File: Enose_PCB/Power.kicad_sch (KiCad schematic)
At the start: 53 parts, among them IC1 ISL91127IRNZ-T7A, IC2 MP2722GRH-0000-Z, J5 USB_C_Receptacle_USB2.0_16P, J6 Battery Terminal, SW3 SW_DPST_x2, U2 USBLC6-4SC6

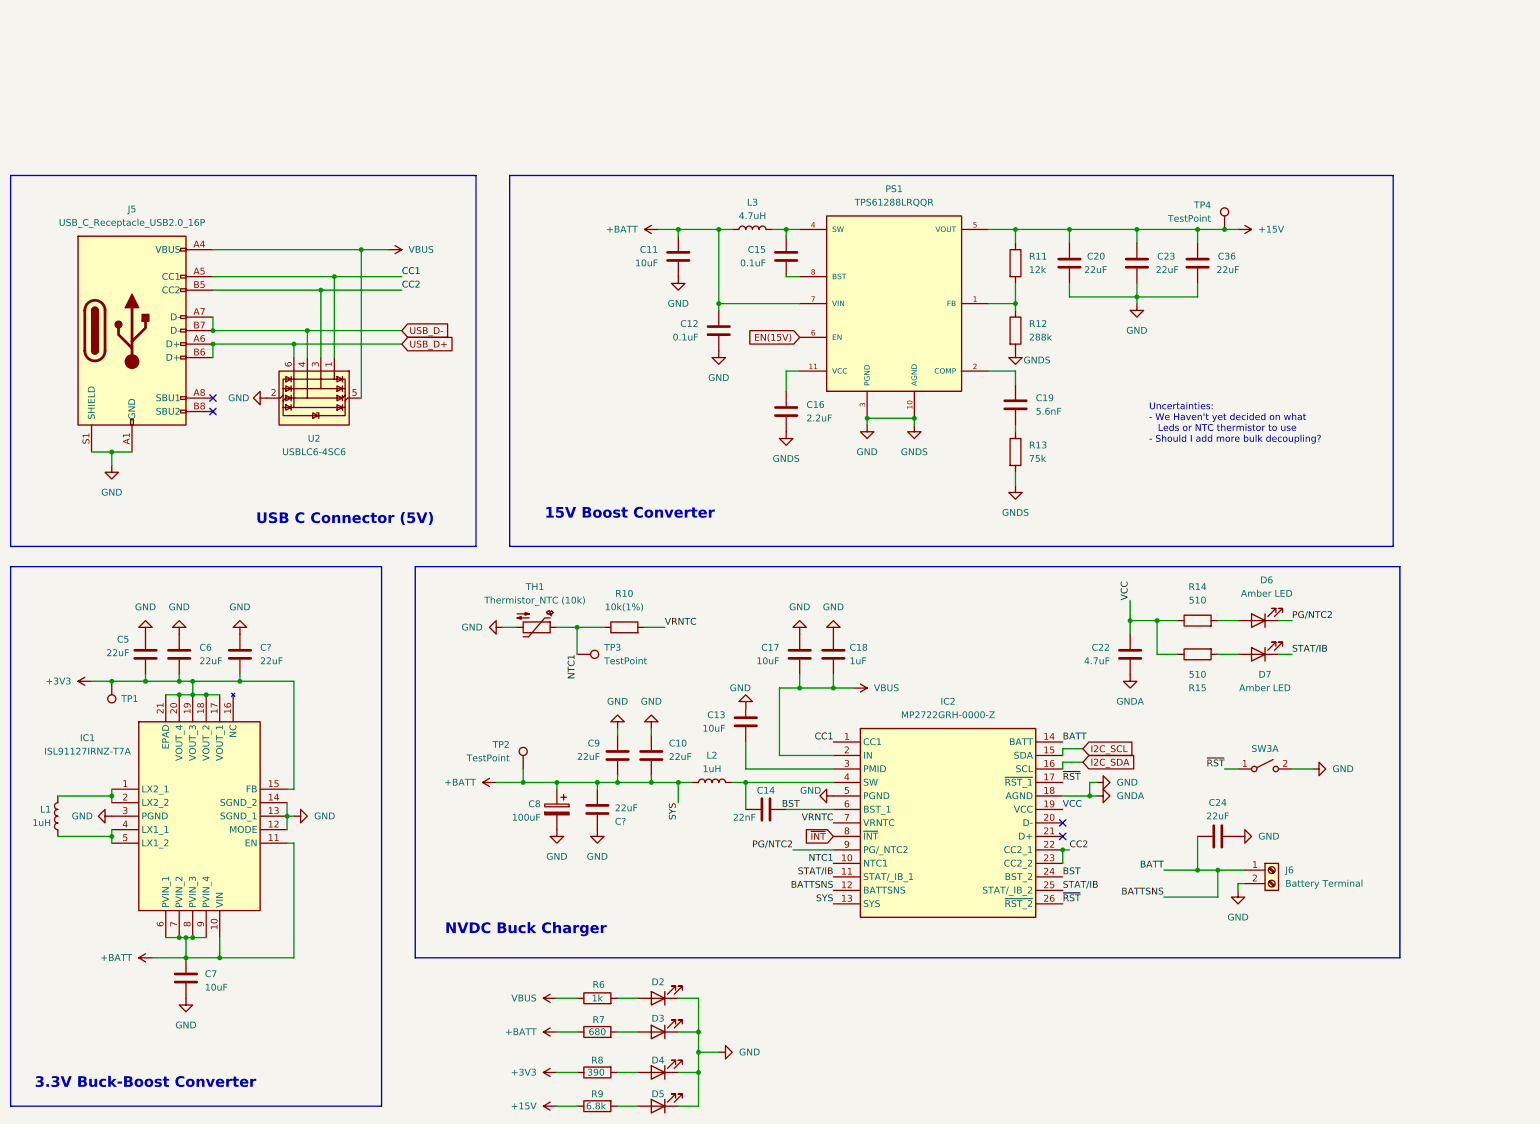
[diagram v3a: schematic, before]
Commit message: Added load switch and stuff
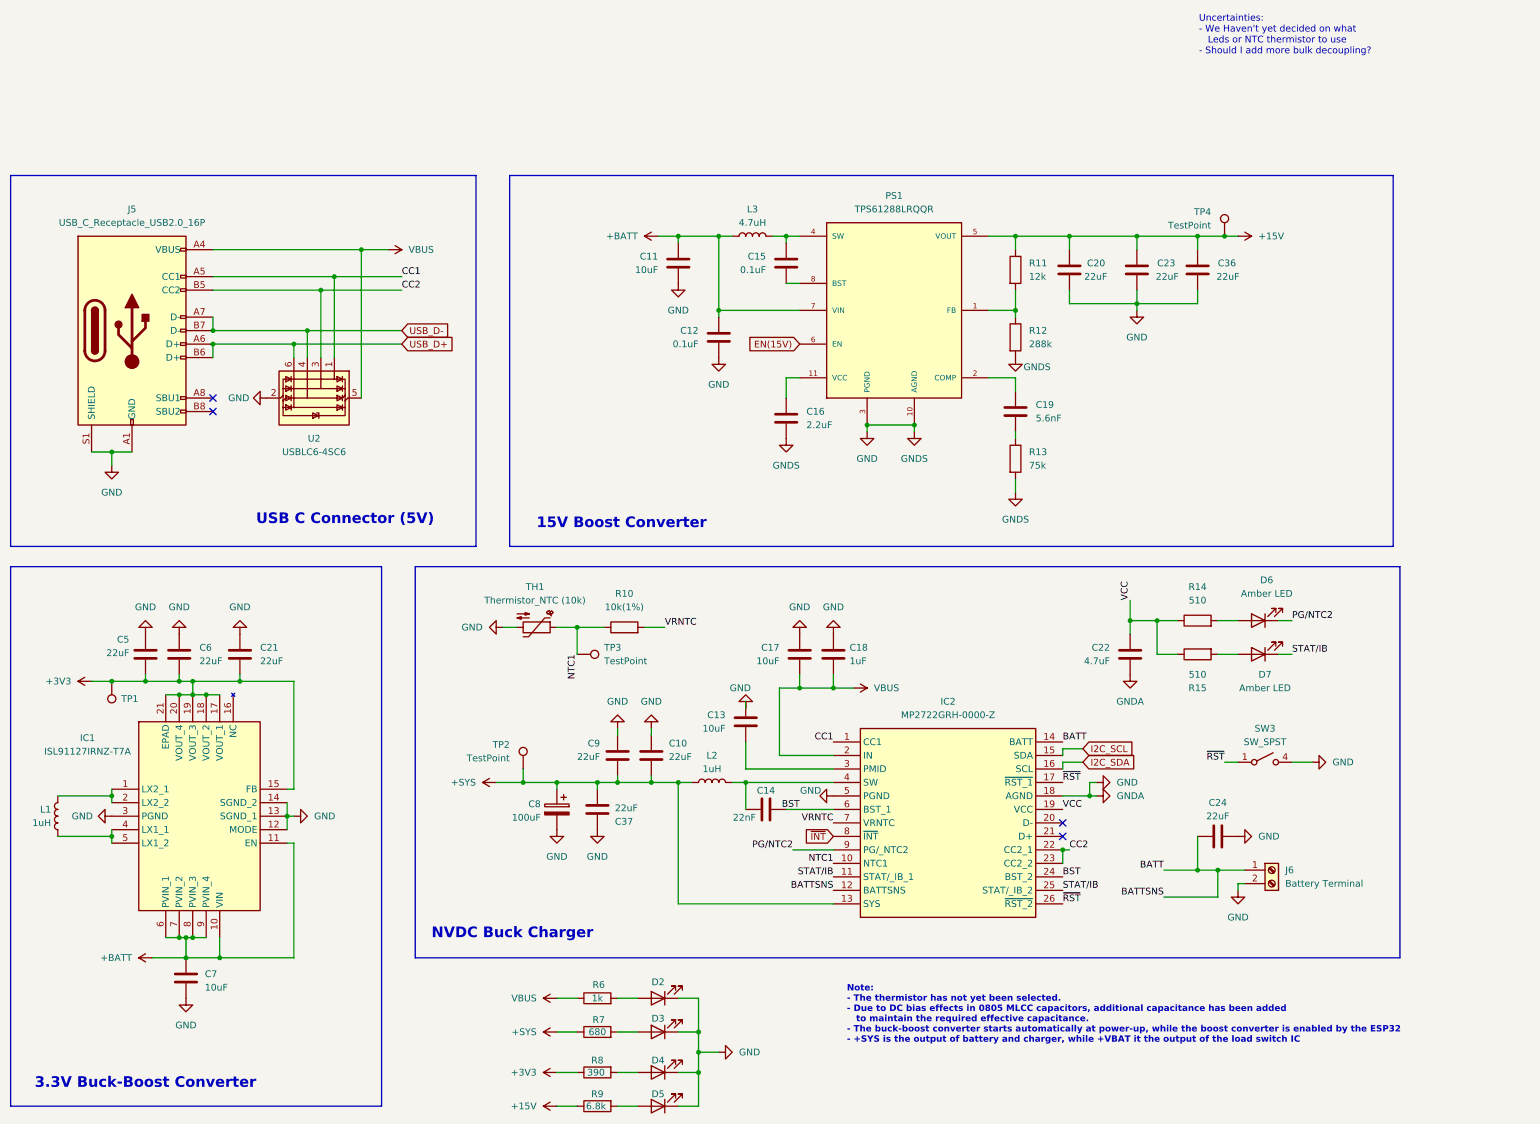
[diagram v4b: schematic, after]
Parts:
- removed SW3: SW_DPST_x2, symbol Switch:SW_DPST_x2
- added SW3: SW_SPST, SamacSys_Parts:430181038816, symbol Switch:SW_SPST
- C10: footprint Capacitor_SMD:C_0805_2012Metric -> Capacitor_SMD:C_0805_2012Metric_Pad1.18x1.45mm_HandSolder
- C11, C12, C13, C14, C15, C16, C17, C18, C19, C22, C24, C5, C6, C7, C9: footprint (none) -> Capacitor_SMD:C_0805_2012Metric_Pad1.18x1.45mm_HandSolder
- C20, C23: footprint Capacitor_SMD:C_1210_3225Metric -> Capacitor_SMD:C_1210_3225Metric_Pad1.33x2.70mm_HandSolder
- C21, C37: renamed from C?; footprint (none) -> Capacitor_SMD:C_0805_2012Metric_Pad1.18x1.45mm_HandSolder
- C36: footprint Capacitor_THT:C_Disc_D6.0mm_W4.4mm_P5.00mm -> Capacitor_SMD:C_1210_3225Metric_Pad1.33x2.70mm_HandSolder
- C8: footprint (none) -> SamacSys_Parts:CAPAE530X610N
- D2, D3, D4, D5, D6, D7: footprint (none) -> LED_SMD:LED_0805_2012Metric_Pad1.15x1.40mm_HandSolder
- IC1: footprint QFN50P400X400X100-21N -> ISL91127IRNZ-T7A:QFN50P400X400X100-21N
- IC2: footprint MP2722GRH0000Z -> SamacSys_Parts:MP2722GRH0000Z
- R10, R11, R12, R13, R14, R15, R6, R7, R8, R9: footprint (none) -> Resistor_SMD:R_0805_2012Metric_Pad1.20x1.40mm_HandSolder
- TP1, TP2, TP3, TP4: footprint (none) -> TestPoint:TestPoint_Pad_1.5x1.5mm
- U2: footprint Package_TO_SOT_SMD:SOT-23-6 -> Package_TO_SOT_SMD:SOT-23-6_Handsoldering
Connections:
- net +BATT: no longer C10.2, C37.1, C8.1, C9.1, IC2.13 (SYS), L2.1, R7.1, TP2.1
- net GND: now also SW3.4 (B)
- net ~{RST}: now also SW3.1 (A)
- new net +SYS: C10.2, C37.1, C8.1, C9.1, IC2.13 (SYS), L2.1, R7.1, TP2.1
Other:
- note added: "Note: - The thermistor has not yet been selected. - Due to DC bias effects in 0805 MLCC capacitors, additional capacitance has been added to maintain the required effective capacitance. - The buck-boost converter starts automatically at power-up, while the boost converter is enabled by the ESP32 - +SYS is the output of battery and charger, while +VBAT it the output of the load switch IC"
- moved on the sheet: C11, C12, C15, C16, C19, C20, C23, C36, L3, PS1, R11, R12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

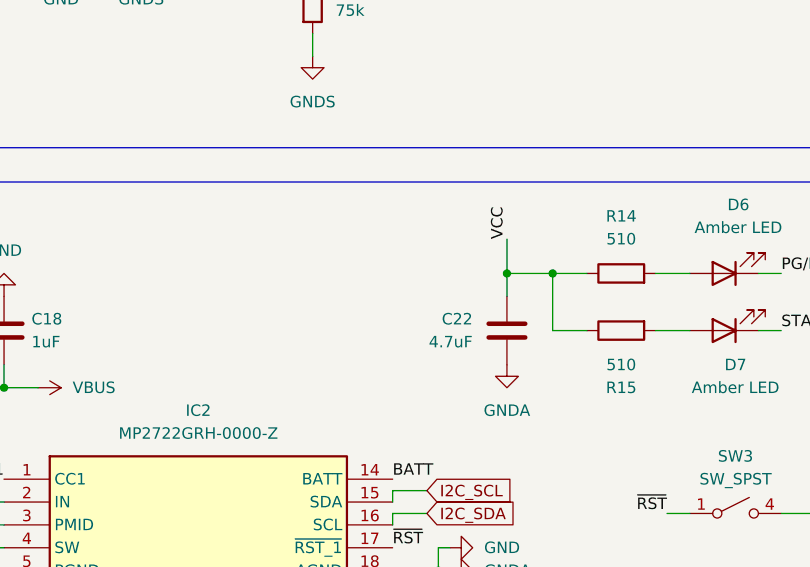
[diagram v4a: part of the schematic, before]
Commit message: Assigned footprints
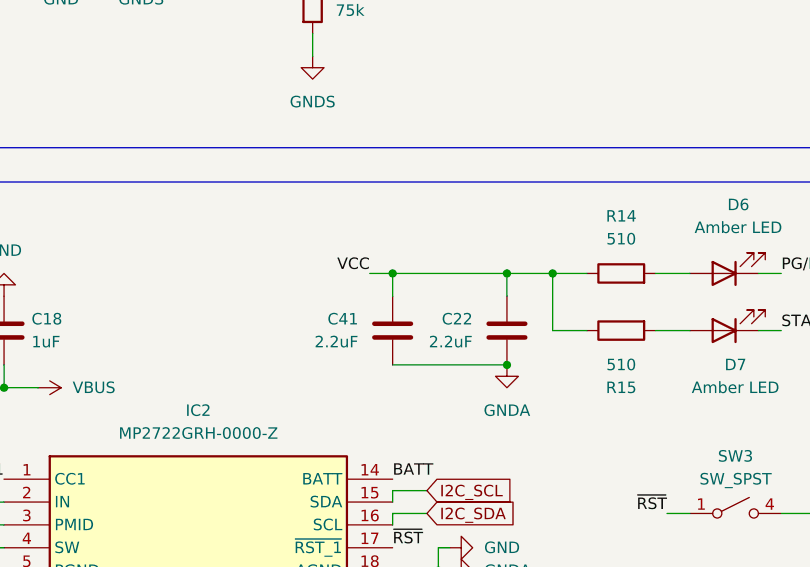
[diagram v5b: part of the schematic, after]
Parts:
- added C41: 2.2uF, Capacitor_SMD:C_0805_2012Metric_Pad1.18x1.45mm_HandSolder, symbol Device:C
- C22: value 4.7uF -> 2.2uF
- J6: footprint (none) -> TerminalBlock_Phoenix:TerminalBlock_Phoenix_PT-1,5-2-3.5-H_1x02_P3.50mm_Horizontal
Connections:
- net GND: now also C41.2
- net VCC: now also C41.1
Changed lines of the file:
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@@
 	)
 	(junction
+		(at 231.14 109.22)
+		(diameter 0)
+		(color 0 0 0 0)
+	)
+	(junction
 		(at 146.05 26.67)
 		(diameter 0)
@@
 	)
 	(junction
+		(at 218.44 99.06)
+		(diameter 0)
+		(color 0 0 0 0)
+	)
+	(junction
 		(at 149.86 176.53)
 		(diameter 0)
@@
 	(wire
 		(pts
+			(xy 218.44 101.6) (xy 218.44 99.06)
+		)
+		(stroke
+			(width 0)
+			(type default)
+		)
+	)
+	(wire
+		(pts
 			(xy 73.66 140.97) (xy 72.39 140.97)
 		)
@@
 	(wire
 		(pts
+			(xy 215.9 99.06) (xy 218.44 99.06)
+		)
+		(stroke
+			(width 0)
+			(type default)
+		)
+	)
+	(wire
+		(pts
 			(xy 156.21 26.67) (xy 153.67 26.67)
 		)
@@
 	(wire
 		(pts
+			(xy 218.44 109.22) (xy 231.14 109.22)
+		)
+		(stroke
+			(width 0)
+			(type default)
+		)
+	)
+	(wire
+		(pts
 			(xy 78.74 36.83) (xy 78.74 49.53)
 		)
@@
 	(wire
 		(pts
-			(xy 231.14 95.25) (xy 231.14 99.06)
+			(xy 73.66 46.99) (xy 73.66 49.53)
 		)
 		(stroke
@@
 	(wire
 		(pts
-			(xy 73.66 46.99) (xy 73.66 49.53)
+			(xy 175.26 109.22) (xy 175.26 111.76)
 		)
 		(stroke
@@
 	(wire
 		(pts
-			(xy 175.26 109.22) (xy 175.26 111.76)
+			(xy 181.61 63.5) (xy 181.61 62.23)
 		)
 		(stroke
@@
 	(wire
 		(pts
-			(xy 181.61 63.5) (xy 181.61 62.23)
+			(xy 218.44 99.06) (xy 231.14 99.06)
 		)
 		(stroke
@@
 	)
 	(label "VCC"
-		(at 231.14 95.25 90)
+		(at 215.9 99.06 180)
 		(effects
 			(font
 				(size 1.27 1.27)
 			)
-			(justify left bottom)
+			(justify right bottom)
 		)
 	)
@@
 			)
 		)
-		(property "Footprint" ""
+		(property "Footprint" "TerminalBlock_Phoenix:TerminalBlock_Phoenix_PT-1,5-2-3.5-H_1x02_P3.50mm_Horizontal"
 			(at 257.81 146.05 0)
 			(effects
@@
 	)
 	(symbol
+		(lib_id "Device:C")
+		(at 218.44 105.41 0)
+		(mirror y)
+		(unit 1)
+		(exclude_from_sim no)
+		(in_bom yes)
+		(on_board yes)
+		(dnp no)
+		(property "Reference" "C41"
+			(at 214.63 104.1399 0)
+			(effects
+				(font
+					(size 1.27 1.27)
+				)
+				(justify left)
+			)
+		)
+		(property "Value" "2.2uF"
+			(at 214.63 106.6799 0)
+			(effects
+				(font
+					(size 1.27 1.27)
+				)
+				(justify left)
+			)
+		)
+		(property "Footprint" "Capacitor_SMD:C_0805_2012Metric_Pad1.18x1.45mm_HandSolder"
+			(at 217.4748 109.22 0)
+			(effects
+				(font
+					(size 1.27 1.27)
+				)
+				(hide yes)
+			)
+		)
+		(property "Datasheet" "~"
+			(at 218.44 105.41 0)
+			(effects
+				(font
+					(size 1.27 1.27)
+				)
+				(hide yes)
+			)
+		)
+		(property "Description" "Unpolarized capacitor"
+			(at 218.44 105.41 0)
+			(effects
+				(font
+					(size 1.27 1.27)
+				)
+				(hide yes)
+			)
+		)
+		(pin "2"
+		)
+		(pin "1"
+		)
+		(instances
+			(project "Enose_PCB"
+				(path "/eef70be0-4107-491c-8ca0-465071a6397e/c704ca63-8ab0-46ce-942e-504221cfea41"
+					(reference "C41")
+					(unit 1)
+				)
+			)
+		)
+	)
+	(symbol
 		(lib_id "Device:R")
 		(at 209.55 68.58 0)
@@
 			)
 		)
-		(property "Value" "4.7uF"
+		(property "Value" "2.2uF"
 			(at 227.33 106.6799 0)
 			(effects
